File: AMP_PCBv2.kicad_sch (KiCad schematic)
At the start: 19 parts, among them U1 Teensy4.0, U2 Adafruit_Feather_M0_RFM9x_LoR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, U2 Logo

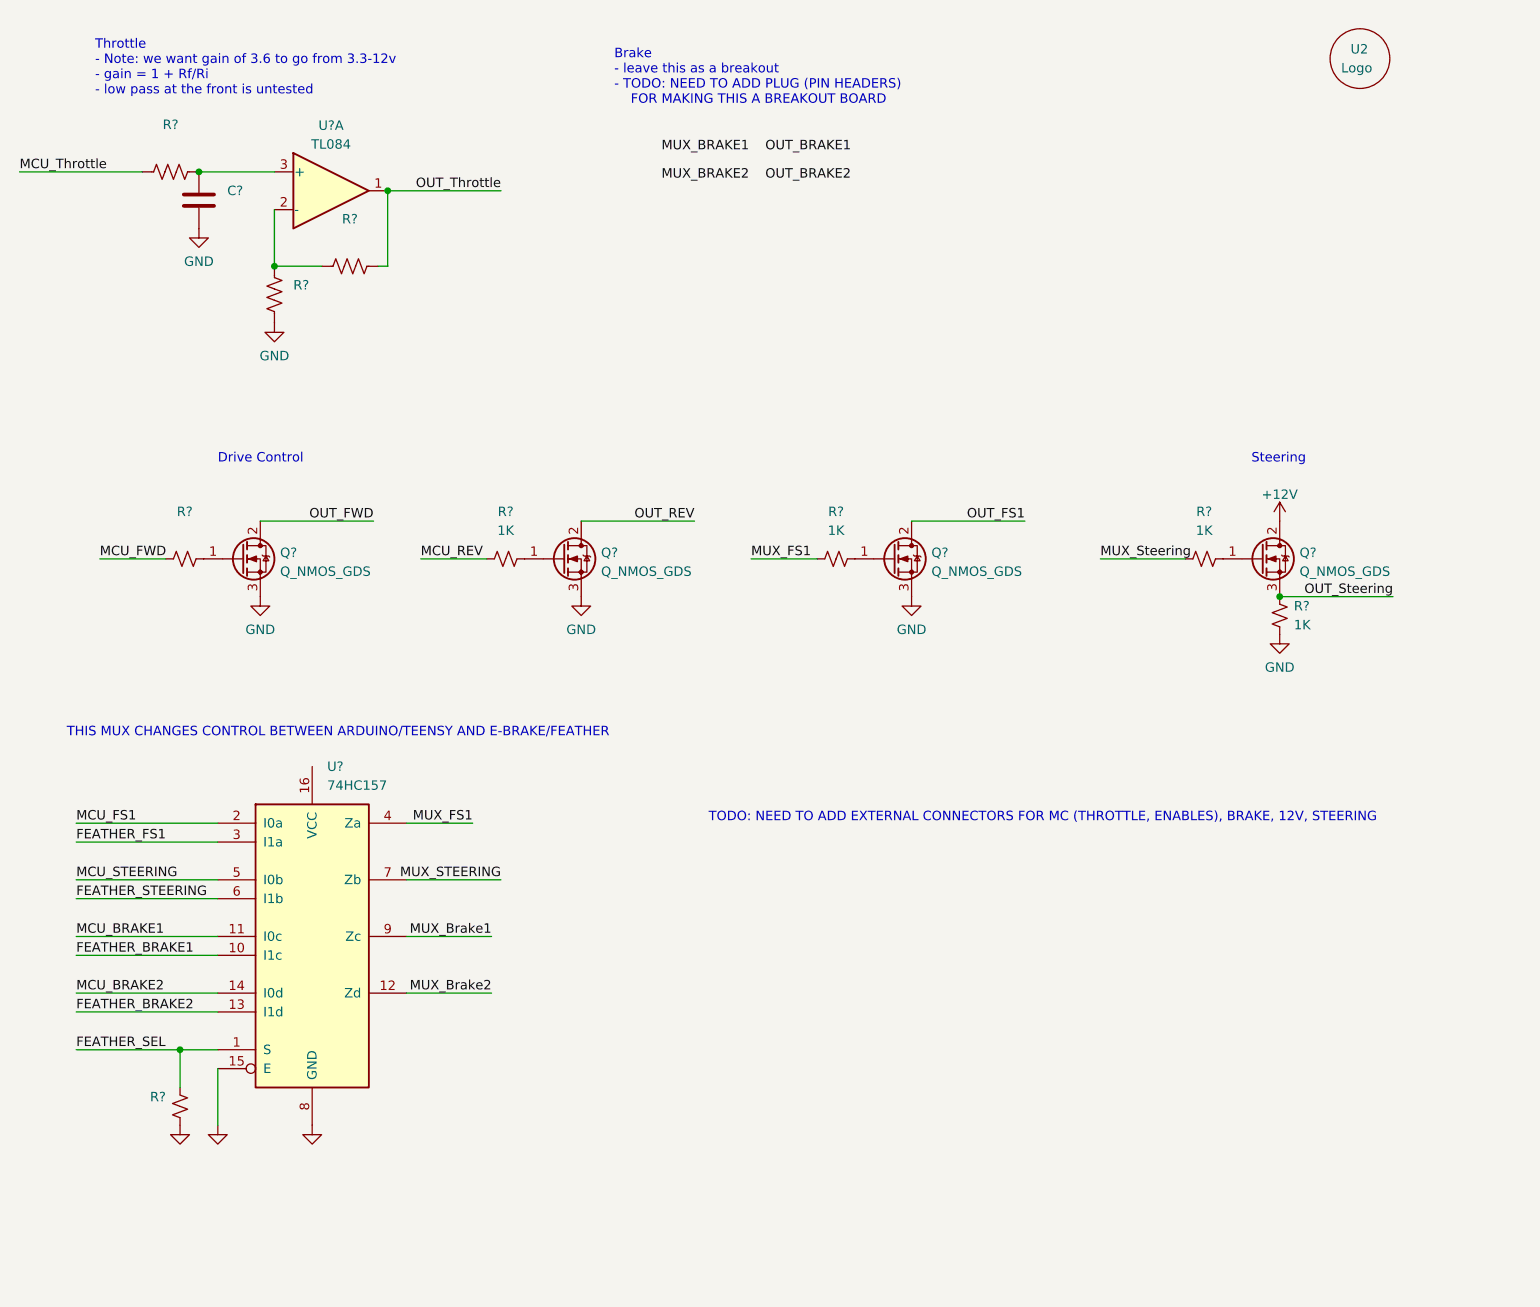
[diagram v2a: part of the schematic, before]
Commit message: Update steering MOSFET configuration
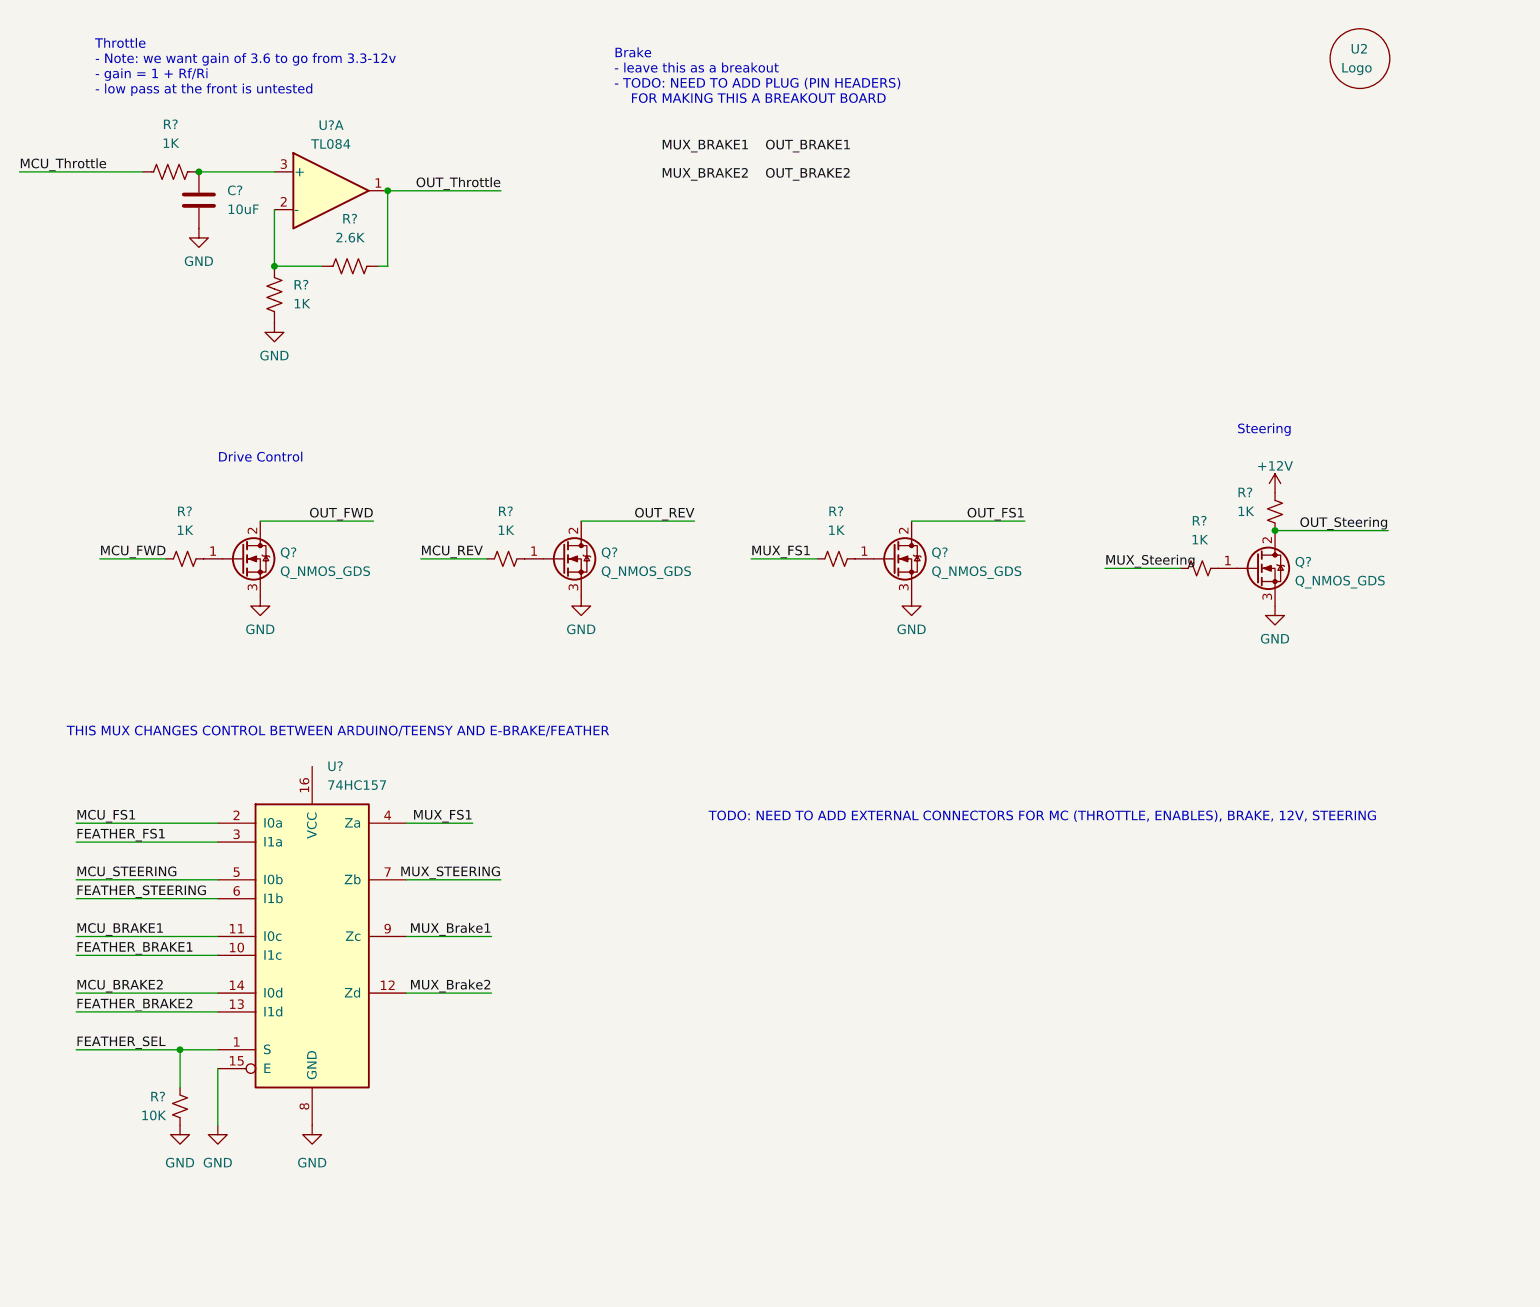
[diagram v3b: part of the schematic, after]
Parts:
- C?: value (none) -> 10uF
- R? (x3): value (none) -> 1K
- R?: value (none) -> 10K
- R?: value (none) -> 2.6K
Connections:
- net +12V: now also R?.2; no longer Q?.2 (D)
- net GND: now also Q?.3 (S); no longer R?.1
- net OUT_Steering: now also Q?.2 (D), R?.1; no longer Q?.3 (S), R?.2
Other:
- moved on the sheet: Q?, R?
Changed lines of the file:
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@@
   (junction (at 139.7 43.18) (diameter 0) (color 0 0 0 0)
   )
-  (junction (at 259.715 97.79) (diameter 0) (color 0 0 0 0)
+  (junction (at 259.08 88.9) (diameter 0) (color 0 0 0 0)
   )
   (junction (at 124.46 53.34) (diameter 0) (color 0 0 0 0)
@@
     (stroke (width 0) (type default) (color 0 0 0 0))
   )
-  (wire (pts (xy 235.585 92.71) (xy 247.015 92.71))
+  (wire (pts (xy 236.22 93.98) (xy 246.38 93.98))
     (stroke (width 0) (type default) (color 0 0 0 0))
   )
@@
     (stroke (width 0) (type default) (color 0 0 0 0))
   )
-  (wire (pts (xy 259.715 97.79) (xy 274.955 97.79))
+  (wire (pts (xy 259.08 88.9) (xy 274.32 88.9))
     (stroke (width 0) (type default) (color 0 0 0 0))
   )
@@
     (effects (font (size 1.27 1.27)) (justify left bottom))
   )
-  (text "Steering" (at 255.905 80.01 0)
+  (text "Steering" (at 254 76.2 0)
     (effects (font (size 1.27 1.27)) (justify left bottom))
   )
@@
     (effects (font (size 1.27 1.27)) (justify left bottom))
   )
-  (label "MUX_Steering" (at 235.585 92.71 0)
+  (label "MUX_Steering" (at 236.22 93.98 0)
     (effects (font (size 1.27 1.27)) (justify left bottom))
   )
@@
     (effects (font (size 1.27 1.27)) (justify left bottom))
   )
-  (label "OUT_Steering" (at 274.955 97.79 180)
+  (label "OUT_Steering" (at 274.32 88.9 180)
     (effects (font (size 1.27 1.27)) (justify right bottom))
   )
@@
     (in_bom yes) (on_board yes) (fields_autoplaced)
     (property "Reference" "R?" (id 0) (at 112.395 86.36 90))
-    (property "Value" "" (id 1) (at 112.395 88.9 90))
+    (property "Value" "1K" (id 1) (at 112.395 88.9 90))
     (property "Footprint" "" (id 2) (at 112.395 92.71 0)
       (effects (font (size 1.27 1.27)) hide)
@@
     (pin "9")
   )
-  (symbol (lib_id "Device:R_Small_US") (at 259.715 100.33 180) (unit 1)
-    (in_bom yes) (on_board yes) (fields_autoplaced)
-    (property "Reference" "R?" (id 0) (at 261.62 99.0599 0)
+  (symbol (lib_id "Device:R_Small_US") (at 259.08 86.36 180) (unit 1)
+    (in_bom yes) (on_board yes)
+    (property "Reference" "R?" (id 0) (at 254 83.82 0)
       (effects (font (size 1.27 1.27)) (justify right))
     )
-    (property "Value" "1K" (id 1) (at 261.62 101.5999 0)
+    (property "Value" "1K" (id 1) (at 254 86.36 0)
       (effects (font (size 1.27 1.27)) (justify right))
     )
-    (property "Footprint" "" (id 2) (at 259.715 100.33 0)
-      (effects (font (size 1.27 1.27)) hide)
-    )
-    (property "Datasheet" "~" (id 3) (at 259.715 100.33 0)
+    (property "Footprint" "" (id 2) (at 259.08 86.36 0)
+      (effects (font (size 1.27 1.27)) hide)
+    )
+    (property "Datasheet" "~" (id 3) (at 259.08 86.36 0)
       (effects (font (size 1.27 1.27)) hide)
     )
@@
       (effects (font (size 1.27 1.27)) hide)
     )
-    (property "Value" "" (id 1) (at 129.54 173.99 0))
+    (property "Value" "GND" (id 1) (at 129.54 173.99 0))
     (property "Footprint" "" (id 2) (at 129.54 168.91 0)
       (effects (font (size 1.27 1.27)) hide)
@@
       (effects (font (size 1.27 1.27)) (justify right))
     )
-    (property "Value" "" (id 1) (at 118.11 45.7199 0)
+    (property "Value" "10uF" (id 1) (at 118.11 45.7199 0)
       (effects (font (size 1.27 1.27)) (justify right))
     )
@@
     (pin "2")
   )
-  (symbol (lib_id "power:GND") (at 259.715 102.87 0) (unit 1)
-    (in_bom yes) (on_board yes) (fields_autoplaced)
-    (property "Reference" "#PWR?" (id 0) (at 259.715 109.22 0)
-      (effects (font (size 1.27 1.27)) hide)
-    )
-    (property "Value" "GND" (id 1) (at 259.715 107.3134 0))
-    (property "Footprint" "" (id 2) (at 259.715 102.87 0)
-      (effects (font (size 1.27 1.27)) hide)
-    )
-    (property "Datasheet" "" (id 3) (at 259.715 102.87 0)
-      (effects (font (size 1.27 1.27)) hide)
-    )
-    (pin "1")
-  )
-  (symbol (lib_id "Device:Q_NMOS_GDS") (at 257.175 92.71 0) (unit 1)
+  (symbol (lib_id "power:GND") (at 259.08 99.06 0) (unit 1)
+    (in_bom yes) (on_board yes) (fields_autoplaced)
+    (property "Reference" "#PWR?" (id 0) (at 259.08 105.41 0)
+      (effects (font (size 1.27 1.27)) hide)
+    )
+    (property "Value" "GND" (id 1) (at 259.08 103.5034 0))
+    (property "Footprint" "" (id 2) (at 259.08 99.06 0)
+      (effects (font (size 1.27 1.27)) hide)
+    )
+    (property "Datasheet" "" (id 3) (at 259.08 99.06 0)
+      (effects (font (size 1.27 1.27)) hide)
+    )
+    (pin "1")
+  )
+  (symbol (lib_id "Device:Q_NMOS_GDS") (at 256.54 93.98 0) (unit 1)
     (in_bom yes) (on_board yes)
-    (property "Reference" "Q?" (id 0) (at 262.382 91.8753 0)
-      (effects (font (size 1.27 1.27)) (justify left))
-    )
-    (property "Value" "Q_NMOS_GDS" (id 1) (at 262.382 94.4122 0)
-      (effects (font (size 1.27 1.27)) (justify left))
-    )
-    (property "Footprint" "" (id 2) (at 262.255 90.17 0)
-      (effects (font (size 1.27 1.27)) hide)
-    )
-    (property "Datasheet" "~" (id 3) (at 257.175 92.71 0)
+    (property "Reference" "Q?" (id 0) (at 261.747 93.1453 0)
+      (effects (font (size 1.27 1.27)) (justify left))
+    )
+    (property "Value" "Q_NMOS_GDS" (id 1) (at 261.747 95.6822 0)
+      (effects (font (size 1.27 1.27)) (justify left))
+    )
+    (property "Footprint" "" (id 2) (at 261.62 91.44 0)
+      (effects (font (size 1.27 1.27)) hide)
+    )
+    (property "Datasheet" "~" (id 3) (at 256.54 93.98 0)
       (effects (font (size 1.27 1.27)) hide)
     )
@@
     (in_bom yes) (on_board yes) (fields_autoplaced)
     (property "Reference" "R?" (id 0) (at 110.49 34.29 90))
-    (property "Value" "" (id 1) (at 110.49 36.83 90))
+    (property "Value" "1K" (id 1) (at 110.49 36.83 90))
     (property "Footprint" "" (id 2) (at 110.744 39.624 90)
       (effects (font (size 1.27 1.27)) hide)
@@
     (pin "9")
   )
-  (symbol (lib_id "power:+12V") (at 259.715 87.63 0) (unit 1)
-    (in_bom yes) (on_board yes) (fields_autoplaced)
-    (property "Reference" "#PWR?" (id 0) (at 259.715 91.44 0)
-      (effects (font (size 1.27 1.27)) hide)
-    )
-    (property "Value" "+12V" (id 1) (at 259.715 84.0542 0))
-    (property "Footprint" "" (id 2) (at 259.715 87.63 0)
-      (effects (font (size 1.27 1.27)) hide)
-    )
-    (property "Datasheet" "" (id 3) (at 259.715 87.63 0)
+  (symbol (lib_id "power:+12V") (at 259.08 83.82 0) (unit 1)
+    (in_bom yes) (on_board yes)
+    (property "Reference" "#PWR?" (id 0) (at 259.08 87.63 0)
+      (effects (font (size 1.27 1.27)) hide)
+    )
+    (property "Value" "+12V" (id 1) (at 259.08 80.2442 0))
+    (property "Footprint" "" (id 2) (at 259.08 83.82 0)
+      (effects (font (size 1.27 1.27)) hide)
+    )
+    (property "Datasheet" "" (id 3) (at 259.08 83.82 0)
       (effects (font (size 1.27 1.27)) hide)
     )
@@
       (effects (font (size 1.27 1.27)) (justify right))
     )
-    (property "Value" "" (id 1) (at 109.855 167.64 0)
+    (property "Value" "10K" (id 1) (at 109.855 167.64 0)
       (effects (font (size 1.27 1.27)) (justify right))
     )
@@
       (effects (font (size 1.27 1.27)) hide)
     )
-    (property "Value" "" (id 1) (at 111.76 173.99 0))
+    (property "Value" "GND" (id 1) (at 111.76 173.99 0))
     (property "Footprint" "" (id 2) (at 111.76 168.91 0)
       (effects (font (size 1.27 1.27)) hide)
@@
       (effects (font (size 1.27 1.27)) (justify left))
     )
-    (property "Value" "" (id 1) (at 127 58.4199 0)
+    (property "Value" "1K" (id 1) (at 127 58.4199 0)
       (effects (font (size 1.27 1.27)) (justify left))
     )
@@
       (effects (font (size 1.27 1.27)) hide)
     )
-    (property "Value" "" (id 1) (at 116.84 173.99 0))
+    (property "Value" "GND" (id 1) (at 116.84 173.99 0))
     (property "Footprint" "" (id 2) (at 116.84 168.91 0)
       (effects (font (size 1.27 1.27)) hide)
@@
     (in_bom yes) (on_board yes) (fields_autoplaced)
     (property "Reference" "R?" (id 0) (at 134.62 46.99 90))
-    (property "Value" "" (id 1) (at 134.62 49.53 90))
+    (property "Value" "2.6K" (id 1) (at 134.62 49.53 90))
     (property "Footprint" "" (id 2) (at 134.874 52.324 90)
       (effects (font (size 1.27 1.27)) hide)
@@
     (pin "2")
   )
-  (symbol (lib_id "Device:R_Small_US") (at 249.555 92.71 90) (unit 1)
-    (in_bom yes) (on_board yes) (fields_autoplaced)
-    (property "Reference" "R?" (id 0) (at 249.555 86.36 90))
-    (property "Value" "1K" (id 1) (at 249.555 88.9 90))
-    (property "Footprint" "" (id 2) (at 249.555 92.71 0)
-      (effects (font (size 1.27 1.27)) hide)
-    )
-    (property "Datasheet" "~" (id 3) (at 249.555 92.71 0)
-      (effects (font (size 1.27 1.27)) hide)
-    )
+  (symbol (lib_id "Device:R_Small_US") (at 248.92 93.98 90) (unit 1)
+    (in_bom yes) (on_board yes) (fields_autoplaced)
+    (property "Reference" "R?" (id 0) (at 248.92 87.63 90))
+    (property "Value" "1K" (id 1) (at 248.92 90.17 90))
+    (property "Footprint" "" (id 2) (at 248.92 93.98 0)
+      (effects (font (size 1.27 1.27)) hide)
+    )
+    (property "Datasheet" "~" (id 3) (at 248.92 93.98 0)
+      (effects (font (size 1.27 1.27)) hide)
+    )
